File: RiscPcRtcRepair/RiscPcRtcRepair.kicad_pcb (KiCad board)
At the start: 2 copper layers, 22 x 32 mm, 11 parts, among them U1 PCF8583, X1 32.768kHz

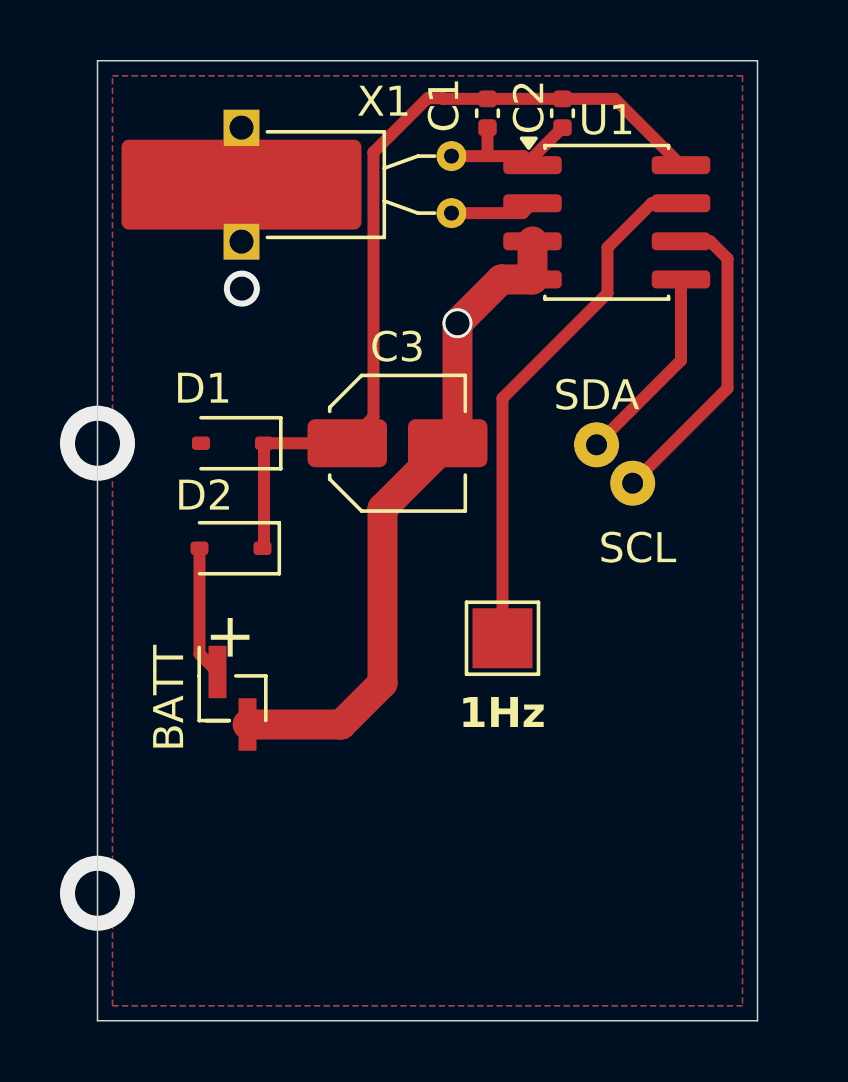
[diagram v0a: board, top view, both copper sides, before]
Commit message: Revision 2 to the RTL board
Fixes all the issues we found:
- wrong footprint
- missing decoupling cap
- new ground castellation
- switched to 0805 for easy soldering
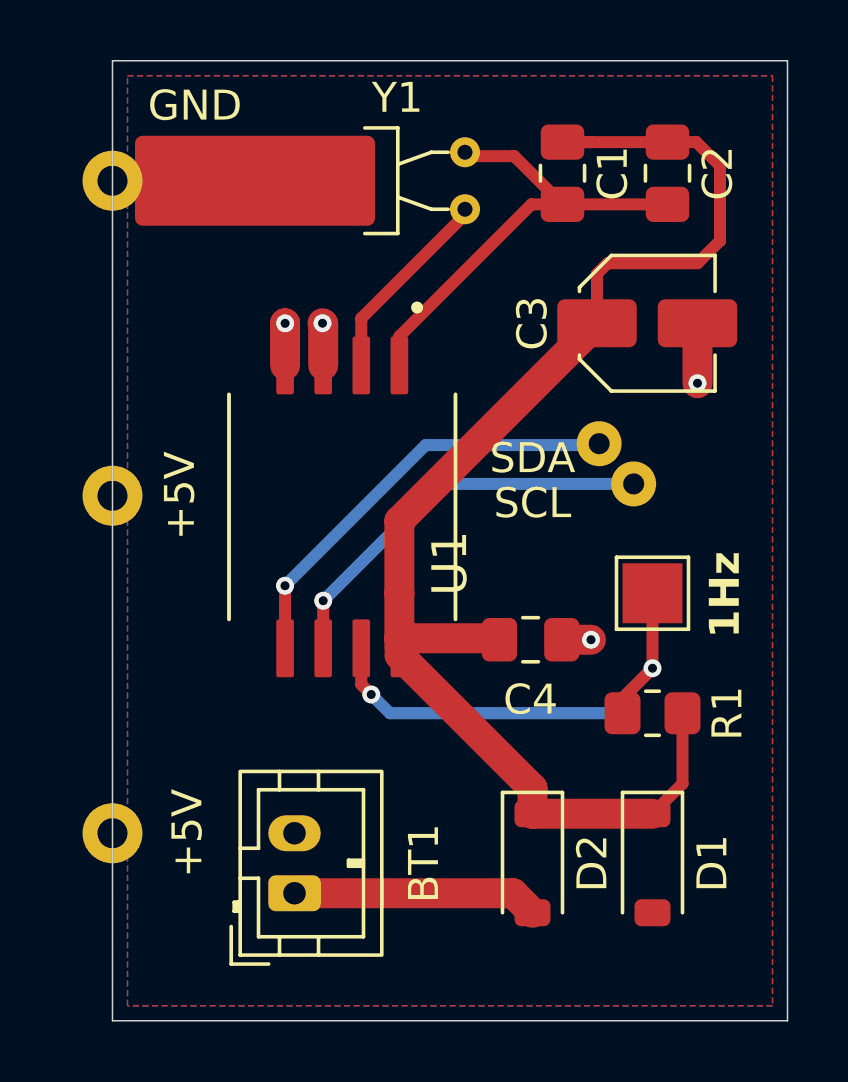
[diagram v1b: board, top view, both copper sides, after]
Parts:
- removed BATT: CR2032, Connector_PinHeader_1.00mm:PinHeader_1x02_P1.00mm_Vertical_SMD_Pin1Right
- removed INT: TestPoint, TestPoint:TestPoint_Pad_2.0x2.0mm
- removed X1: 32.768kHz, Crystal:Crystal_C38-LF_D3.0mm_L8.0mm_Horizontal_1EP_style2
- added +5V: TestPoint, TestPoint:TestPoint_THTPad_D2.0mm_Drill1.0mm, F.Cu at (93.0, 81.2)
- added +5V2: TestPoint, TestPoint:TestPoint_THTPad_D2.0mm_Drill1.0mm, F.Cu at (93.0, 92.5)
- added BT1: CR2032, Connector_JST:JST_PH_B2B-PH-K_1x02_P2.00mm_Vertical, F.Cu at (99.1, 94.5)
- added C4: C, Capacitor_SMD:C_0805_2012Metric_Pad1.18x1.45mm_HandSolder, F.Cu at (106.9, 86.0)
- added GND: TestPoint, TestPoint:TestPoint_THTPad_D2.0mm_Drill1.0mm, F.Cu at (93.0, 70.8)
- added INT1: TestPoint, TestPoint:TestPoint_Pad_2.0x2.0mm, F.Cu at (111.0, 84.5)
- added R1: 4k7, Resistor_SMD:R_0805_2012Metric_Pad1.20x1.40mm_HandSolder, F.Cu at (111.0, 88.5)
- added Y1: Crystal_GND3, Crystal:Crystal_C38-LF_D3.0mm_L8.0mm_Horizontal_1EP_style1, F.Cu at (104.8, 69.8)
- C1, C2: footprint Capacitor_SMD:C_0402_1005Metric -> Capacitor_SMD:C_0805_2012Metric_Pad1.18x1.45mm_HandSolder
- D1, D2: value BAT85 -> BAT46W; footprint Diode_SMD:D_SOD-323 -> Diode_SMD:D_SOD-123
- U1: value PCF8583 -> PCF8583T; footprint Package_SO:SOIC-8_3.9x4.9mm_P1.27mm -> Local:SOIC127P1032X265-8N
- moved D1 19.8 mm to (111.0, 93.5), turned to -90 degrees
- moved D2 14.5 mm to (107.0, 93.5), turned to -90 degrees
- moved U1 13.0 mm to (100.7, 81.6), turned to -90 degrees
- moved C3 9.24 mm to (110.8, 75.5)
- moved C2 4.03 mm to (111.5, 70.5)
- moved C1 3.20 mm to (108.0, 70.5)
- moved SDA 0.09 mm to (109.2, 79.5)
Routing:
- net Net-(D1-K): track 28.3 -> 48.2 mm
- net GND: track 22.5 -> 5.80 mm, vias 2 -> 4
- net Net-(U1-OSCI): track 5.44 -> 15.6 mm
- net Net-(U1-SDA): track 6.68 -> 14.5 mm, vias 0 -> 1
- net Net-(BT1-+): track 4.37 -> 8.20 mm
- net Net-(U1-OSCO): track 2.84 -> 6.53 mm
- net Net-(U1-SCL): track 10.6 -> 13.5 mm, vias 0 -> 1
- net Net-(U1-~{INT}): track 17.5 -> 16.3 mm, vias 0 -> 2
- net +5V: vias 2 -> 0
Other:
- board size 22 x 32 mm -> 22.5 x 32 mm
- board text added: "+5V"

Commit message: Fix warnings and add gerbers
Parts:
- Y1: footprint Crystal:Crystal_C38-LF_D3.0mm_L8.0mm_Horizontal_1EP_style1 -> Crystal:Crystal_C26-LF_D2.1mm_L6.5mm_Horizontal_1EP_style2
- moved C3 0.11 mm to (107.0, 86.0)
- renumbered +5V2 to +5V1, BT1 to BT, C4 to C3, C3 to C4
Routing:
- net GND: track 5.80 -> 11.1 mm
- net Net-(D1-K): track 48.2 -> 47.2 mm
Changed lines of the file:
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@@
 		(tags "test point THT pad")
 		(property "Reference" "GND"
-			(at 2.75 -2.5 0)
+			(at 1.881715 0 90)
 			(layer "F.SilkS")
 			(effects
@@
 			(pinfunction "1")
 			(pintype "passive")
+			(zone_connect 2)
 		)
 		(embedded_fonts no)
@@
 		(descr "SMD capacitor, aluminum electrolytic nonpolar, 4.0x5.4mm")
 		(tags "capacitor electrolytic nonpolar")
-		(property "Reference" "C3"
+		(property "Reference" "C4"
 			(at -3.825 0 90)
 			(layer "F.SilkS")
@@
 		)
 	)
-	(footprint "Crystal:Crystal_C38-LF_D3.0mm_L8.0mm_Horizontal_1EP_style1"
+	(footprint "Crystal:Crystal_C26-LF_D2.1mm_L6.5mm_Horizontal_1EP_style2"
 		(layer "F.Cu")
 		(at 104.75 69.8 -90)
-		(descr "C38-LF, Crystal, length 8.0mm, width 3.0mm, THT")
+		(descr "C26-LF, Crystal, length 6.5mm, width 2.1mm, THT")
 		(property "Reference" "Y1"
-			(at -1.81 2.25 0)
+			(at -1.59 1.75 0)
 			(layer "F.SilkS")
 			(effects
@@
 		)
 		(property "Value" "Crystal_GND3"
-			(at 3.71 2.25 0)
+			(at 3.49 1.75 0)
 			(layer "F.Fab")
 			(effects
@@
 			)
 		)
-		(property "Datasheet" "~"
-			(at 0 0 90)
+		(property "Datasheet" ""
+			(at 0 0 270)
 			(layer "F.Fab")
 			(hide yes)
@@
 			)
 		)
-		(property "Description" "Three pin crystal, GND on pin 3"
-			(at 0 0 90)
+		(property "Description" ""
+			(at 0 0 270)
 			(layer "F.Fab")
 			(hide yes)
@@
 		(attr through_hole)
 		(fp_line
-			(start -0.81 3.34)
-			(end -0.81 2.24)
+			(start -0.41 4.89)
+			(end -0.41 1.74)
 			(stroke
 				(width 0.12)
@@
 		)
 		(fp_line
-			(start -0.81 2.24)
-			(end 2.71 2.24)
+			(start -0.41 1.74)
+			(end 2.31 1.74)
 			(stroke
 				(width 0.12)
@@
 		)
 		(fp_line
-			(start 0.405 2.24)
-			(end 0 1.12)
+			(start 0.6 1.74)
+			(end 0 0.87)
 			(stroke
 				(width 0.12)
@@
 		)
 		(fp_line
-			(start 1.495 2.24)
-			(end 1.9 1.12)
+			(start 1.3 1.74)
+			(end 1.9 0.87)
 			(stroke
 				(width 0.12)
@@
 		)
 		(fp_line
-			(start 2.71 2.24)
-			(end 2.71 3.34)
+			(start 2.31 1.74)
+			(end 2.31 4.89)
 			(stroke
 				(width 0.12)
@@
 		)
 		(fp_line
-			(start 0 1.12)
+			(start 0 0.87)
 			(end 0 0.56)
 			(stroke
@@
 		)
 		(fp_line
-			(start 1.9 1.12)
+			(start 1.9 0.87)
 			(end 1.9 0.56)
 			(stroke
@@
 		)
 		(fp_rect
-			(start -1.3 -0.75)
-			(end 3.2 11.25)
+			(start -1.4 -0.75)
+			(end 3.3 9.25)
 			(stroke
 				(width 0.05)
@@
 		)
 		(fp_line
-			(start 0.405 2.5)
-			(end 0 1.25)
+			(start -0.55 5.75)
+			(end 2.45 5.75)
 			(stroke
 				(width 0.1)
@@
 		)
 		(fp_line
-			(start 1.495 2.5)
-			(end 1.9 1.25)
+			(start 0.6 2)
+			(end 0 1)
 			(stroke
 				(width 0.1)
@@
 		)
 		(fp_line
-			(start 0 1.25)
+			(start 1.3 2)
+			(end 1.9 1)
+			(stroke
+				(width 0.1)
+				(type solid)
+			)
+			(layer "F.Fab")
+		)
+		(fp_line
+			(start 0 1)
 			(end 0 0)
 			(stroke
@@
 		)
 		(fp_line
-			(start 1.9 1.25)
+			(start 1.9 1)
 			(end 1.9 0)
 			(stroke
@@
 		)
 		(fp_rect
-			(start -0.55 2.5)
-			(end 2.45 10.5)
+			(start -0.08 2)
+			(end 1.98 8.5)
 			(stroke
 				(width 0.1)
@@
 		)
 		(fp_text user "${REFERENCE}"
-			(at 0.95 6.45 0)
+			(at 0.95 5.25 0)
 			(layer "F.Fab")
 			(effects
@@
 			(pintype "passive")
 		)
+		(pad "3" thru_hole rect
+			(at -0.55 5.75 270)
+			(size 1.2 1.2)
+			(drill 0.8)
+			(layers "*.Cu" "*.Mask")
+			(remove_unused_layers no)
+			(net 2 "GND")
+			(pinfunction "3")
+			(pintype "passive")
+		)
 		(pad "3" smd roundrect
-			(at 0.95 7 270)
-			(size 3 8)
+			(at 0.95 5.75 270)
+			(size 2.2 6.5)
 			(layers "F.Cu" "F.Mask" "F.Paste")
-			(roundrect_rratio 0.083333)
+			(roundrect_rratio 0.113636)
+			(net 2 "GND")
+			(pinfunction "3")
+			(pintype "passive")
+		)
+		(pad "3" thru_hole rect
+			(at 2.45 5.75 270)
+			(size 1.2 1.2)
+			(drill 0.8)
+			(layers "*.Cu" "*.Mask")
+			(remove_unused_layers no)
 			(net 2 "GND")
 			(pinfunction "3")
@@
 		)
 		(embedded_fonts no)
-		(model "${KICAD9_3DMODEL_DIR}/Crystal.3dshapes/Crystal_C38-LF_D3.0mm_L8.0mm_Horizontal_1EP_style1.step"
+		(model "${KICAD9_3DMODEL_DIR}/Crystal.3dshapes/Crystal_C26-LF_D2.1mm_L6.5mm_Horizontal_1EP_style2.step"
 			(offset
 				(xyz 0 0 0)
@@
 		(descr "JST PH series connector, B2B-PH-K (http://www.jst-mfg.com/product/pdf/eng/ePH.pdf), generated with kicad-footprint-generator")
 		(tags "connector JST PH vertical")
-		(property "Reference" "BT1"
+		(property "Reference" "BT"
 			(at 1 4.318777 90)
 			(layer "F.SilkS")
@@
 			(pinfunction "-")
 			(pintype "passive")
+			(zone_connect 2)
 		)
 		(embedded_fonts no)
@@
 		(descr "THT pad as test Point, diameter 2.0mm, hole diameter 1.0mm")
 		(tags "test point THT pad")
-		(property "Reference" "+5V2"
+		(property "Reference" "+5V1"
 			(at 1.5 -3 90)
 			(layer "F.SilkS")
@@
 		(at 100.658166 81.620968 -90)
 		(property "Reference" "U1"
-			(at 1.879032 -3.591834 270)
+			(at 2.329032 -5.341834 0)
 			(layer "F.SilkS")
 			(effects
@@
 	(footprint "Capacitor_SMD:C_0805_2012Metric_Pad1.18x1.45mm_HandSolder"
 		(layer "F.Cu")
-		(at 106.9375 86.05 180)
+		(at 107.05 86.05 180)
 		(descr "Capacitor SMD 0805 (2012 Metric), square (rectangular) end terminal, IPC-7351 nominal with elongated pad for handsoldering. (Body size source: IPC-SM-782 page 76, https://www.pcb-3d.com/wordpress/wp-content/uploads/ipc-sm-782a_amendment_1_and_2.pdf, https://docs.google.com/spreadsheets/d/1BsfQQcO9C6DZCsRaXUlFlo91Tg2WpOkGARC1WS5S8t0/edit?usp=sharing), generated with kicad-footprint-generator")
 		(tags "capacitor handsolder")
-		(property "Reference" "C4"
+		(property "Reference" "C3"
 			(at 0 -2 0)
 			(layer "F.SilkS")
@@
 	)
 	(segment
-		(start 100.023166 76.905968)
-		(end 100.023166 75.523166)
+		(start 107.975 86.05)
+		(end 109.05 86.05)
 		(width 1)
 		(layer "F.Cu")
@@
 	)
 	(segment
-		(start 107.975 86.05)
-		(end 108.95 86.05)
+		(start 99 70.75)
+		(end 93.8 70.75)
+		(width 1)
+		(layer "F.Cu")
+		(net 2)
+	)
+	(segment
+		(start 100.023166 76.905968)
+		(end 100.023166 75.523166)
 		(width 1)
 		(layer "F.Cu")
@@
 	)
 	(via
-		(at 108.95 86.05)
+		(at 100 75.5)
 		(size 0.6)
 		(drill 0.3)
@@
 	)
 	(via
-		(at 100 75.5)
+		(at 109.05 86.05)
 		(size 0.6)
 		(drill 0.3)
@@
 	(segment
 		(start 102.563166 82.086834)
-		(end 109.15 75.5)
+		(end 102.563166 84.5)
 		(width 1)
 		(layer "F.Cu")
@@
 	)
 	(segment
-		(start 105.7875 86)
-		(end 102.563166 86)
+		(start 102.563166 82.086834)
+		(end 109.15 75.5)
 		(width 1)
 		(layer "F.Cu")
@@
 	)
 	(segment
-		(start 108 69.4625)
-		(end 108.9625 69.4625)
-		(width 0.4)
+		(start 105.7875 86)
+		(end 102.563166 86)
+		(width 1)
 		(layer "F.Cu")
 		(net 4)
@@
 	)
 	(segment
-		(start 102.600666 84.4625)
-		(end 102.563166 84.5)
-		(width 0.4)
-		(layer "F.Cu")
-		(net 4)
-	)
-	(segment
 		(start 102.563166 86.563166)
 		(end 107 91)
 		(width 1)
 		(layer "F.Cu")
-		(net 4)
-	)
-	(segment
-		(start 102.563166 84.5)
-		(end 102.563166 82.086834)
-		(width 1)
-		(layer "F.Cu")
